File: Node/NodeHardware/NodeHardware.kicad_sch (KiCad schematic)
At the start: 61 parts, among them J1 USB_C_Receptacle_USB2.0_16P, J2 PWR, J3 BATT, Q1 AO3401A, Q2 AO3401A, U1 TPS565201DDCR, U2 TPS565201DDCR, U3 CH340C, U4 TLV70433DBVR, U5 MCP73831-2-OT

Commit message: Finish all the basic SCHM needed for the ESP32
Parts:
- removed C11, C4: C_, symbol Device:C_Polarized
- removed C13, C2, C9: C, Capacitor_SMD:C_0805_2012Metric, symbol Device:C
- removed D4: 5V1, Diode_SMD:D_SOD-123, symbol Device:D_Zener
- removed JP1, JP2, JP3, JP4, JP5, JP6, JP7, JP8: SolderJumper_2_Bridged, Jumper:SolderJumper-2_P1.3mm_Bridged2Bar_RoundedPad1.0x1.5mm, symbol Jumper:SolderJumper_2_Bridged
- removed Q2: AO3401A, Package_TO_SOT_SMD:SOT-23, symbol Transistor_FET:AO3401A
- removed R12: R, Resistor_SMD:R_0805_2012Metric, symbol Device:R
- added C11, C19, C4: 1u, Capacitor_SMD:C_0805_2012Metric, symbol Device:C
- added C2, C9: 100u, symbol Device:C_Polarized
- added C20: 100n, Capacitor_SMD:C_0805_2012Metric, symbol Device:C
- added C22, C23: 4u7, Capacitor_SMD:C_0805_2012Metric, symbol Device:C
- added D12: 5V1, Diode_SMD:D_SOD-123, symbol Device:D_Zener
- added D4: BLUE, LED_SMD:LED_1210_3225Metric, symbol Device:LED
- added J4: ESP32_JTAG, symbol Connector_Generic:Conn_01x07
- added Q5: AO3401A, Package_TO_SOT_SMD:SOT-23, symbol Transistor_FET:AO3401A
- added R15, R18: 47k, Resistor_SMD:R_0805_2012Metric, symbol Device:R
- added R25, R26, R28, R30, R31, R32, R33, R40: 0R, Resistor_SMD:R_0805_2012Metric, symbol Device:R
- added R27: 4k7, Resistor_SMD:R_0805_2012Metric, symbol Device:R
- added R29: 10k, Resistor_SMD:R_0805_2012Metric, symbol Device:R
- C1, C12, C8: value C -> 100n
- C10, C3, C6: value C -> 10u
- C5: value C_ -> 100u
- C7: value C -> 1u
- D2: Part Name (none) -> BZT52C4V7
- H1, H2, H3, H4: footprint (none) -> MountingHole:MountingHole_3.2mm_M3_Pad_Via
- J1: value USB_C_Receptacle_USB2.0_16P -> USB_C_Receptacle_16P
- L1, L2: value L -> 3.3uH
- R1, R4, R9: value R -> 10k
- R10, R11: value R -> 5k1
- R2: value R -> 54.9k
- R3: value R -> 0R; Use Case (none) -> JUMPER
- R5: value R -> 47k
- R6: value R -> ???
- R7: value R -> 4k7
- R8: value R -> 2k2
- TP1: value TestPoint -> 5V_TP
- TP2: value TestPoint -> V_IN_TP
- TP3: value TestPoint -> GND_TP_1
- TP4: value TestPoint -> GND_TP_2
- TP5: value TestPoint -> GND_TP_3
- TP6: value TestPoint -> GND_TP_4
- TP7: value TestPoint -> 3V3_TP
- TP8: value TestPoint -> 3V3_LP_TP
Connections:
- net BATT_N is gone; now on net GND: J3.1 (Pin_1)
- net PWR_IN_N is gone; now on net GND: J2.1 (Pin_1)
- net +5V: now also C3.1, D1.2 (A), L1.2, R2.1, R3.2, TP1.1, U5.4 (V_{DD}), C2.1, C23.1, C4.1, D4.2 (A), R25.1
- net +BATT: now also U5.3 (V_{BAT}), C20.1, C22.1, D12.1 (K), Q5.2 (S), R28.1
- net BATT_P: now also Q5.3 (D)
- net GND: now also C10.2, C12.2, C3.2, C5.2, C6.2, C7.2, H1.1, H2.1, H3.1, H4.1, J1.A1 (GND), J1.A12 (GND), J1.B1 (GND), J1.B12 (GND), R10.2, R11.2, R4.2, R5.2, R7.2, R9.2, TP3.1, TP4.1, TP5.1, TP6.1, U1.1 (GND), U2.1 (GND), U3.1 (GND), U4.1 (GND), U5.2 (V_{SS}), C11.2, C19.2, C2.2, C20.2, C22.2, C23.2, C4.2, C9.2, J4.1 (Pin_1), R15.2, R18.2, R27.2
- net PWR_IN_P: now also Q1.3 (D)
- net VBUS: now also J1.A4 (VBUS), J1.A9 (VBUS), J1.B4 (VBUS), J1.B9 (VBUS), R3.1
- net V_IN: now also C5.1, C6.1, C7.1, D2.1 (K), Q1.2 (S), TP2.1, R26.1
- net net_lable: now also U3.2 (TXD), U3.3 (RXD), U4.2 (IN), R28.2, R32.1, R33.1
- net +3V3_LP: now reaches TP8.1
- net +3V3_LP: now also U4.3 (OUT), C19.1
- net 3V3_REG_VFB: now reaches R9.1
- net 3V3_REG_VFB: now also R6.2, U2.4 (VFB)
- net +3V3: now reaches TP7.1
- net +3V3: now also C10.1, C12.1, D3.2 (A), L2.2, R6.1, U3.16 (VCC), U3.4 (V3), C11.1, C9.1, J4.7 (Pin_7)
- net PWR_IN_ZENER: now reaches R5.1
- net PWR_IN_ZENER: now also D2.2 (A), Q1.1 (G)
- net 5V_REG_VFB: now reaches R4.1
- net 5V_REG_VFB: now also R2.2, U1.4 (VFB)
- net at R10.1: now also J1.A5 (CC1)
- net 3V3_REG_SW: now reaches U2.2 (SW)
- net 3V3_REG_SW: now also C8.1, L2.1
- net 3V3_REG_IN: now reaches U2.3 (VIN)
- net 3V3_REG_IN: now also R25.2, R29.1
- net 3V3_REG_EN: now reaches U2.5 (EN)
- net 3V3_REG_EN: now also R29.2
- net at U2.6 (VBST): now also C8.2
- net 5V_REG_SW: now reaches U1.2 (SW)
- net 5V_REG_SW: now also C1.1, L1.1
- net 5V_REG_IN: now reaches U1.3 (VIN)
- net 5V_REG_IN: now also R1.1, R26.2
- net 5V_REG_EN: now reaches U1.5 (EN)
- net 5V_REG_EN: now also R1.2
- net at U1.6 (VBST): now also C1.2
- net at R8.1: now also U5.1 (STAT)
- net BATT_LED_K: now reaches R8.2
- net BATT_LED_K: now also D4.1 (K)
- net 5V_REG_LED_K: now reaches D1.1 (K)
- net 5V_REG_LED_K: now also R27.1
- net CH340_DTR: now reaches U3.13 (~{DTR})
- net CH340_RTS: now reaches U3.14 (~{RTS})
- net CH340_USB_D+: now reaches U3.5 (UD+)
- net CH340_USB_D+: now also R30.2
- net CH340_USB_D-: now reaches U3.6 (UD-)
- net CH340_USB_D-: now also R31.2
- net 3V3_REG_LED_K: now reaches D3.1 (K)
- net 3V3_REG_LED_K: now also R7.1
- net at U5.5 (PROG): now also R40.1
- net at R11.1: now also J1.B5 (CC2)
- net USB_D+: now reaches J1.A6 (D+), J1.B6 (D+)
- net USB_D+: now also R30.1
- net USB_D-: now reaches J1.A7 (D-), J1.B7 (D-)
- net USB_D-: now also R31.1
- new net: R18.1, R40.2
- new net BATT_IN_ZENER: D12.2 (A), Q5.1 (G), R15.1
- new net JTAG_RST: J4.6 (Pin_6)
- new net JTAG_TCK: J4.5 (Pin_5)
- new net JTAG_TDI: J4.3 (Pin_3)
- new net JTAG_TDO: J4.4 (Pin_4)
- new net JTAG_TMS: J4.2 (Pin_2)
- new net UART_UC_RX: R32.2
- new net UART_UC_TX: R33.2
- no-connect marks 3 -> 11
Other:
- note added: "3V3 BUCK REGULATOR"
- note added: "5V BUCK REGULATOR"
- note added: "Charging can be disabled by removing the PROG jumper. Charging current regulated by PROG resistor: I_reg = 1000V / R_prog (where R_prog is in kOhm) So for 500mA charging, we need 2kOhm resistor."
- note added: "Charging indicator"
- note added: "Debug connection"
- note added: "Low power 3V3 regulator"
- note added: "Power inputs"
- note added: "TODO: Screw terminal (or similar) output pins, with LED indicators of activation (all selectable with one jumper - so we can disable it for ultra low power mode)"
- note added: "TODO: add a symbol and footprint for logo"
- note added: "TODO: add jumpers for power connections for ICs, and jumpers to be able to disconnect anything if needed!"
- note added: "USB C Connector"
- note added: "USB TO UART"
- note added: "Up to 150mA @ 3V3 (3.4μA quiescent current)"
- note added: "What batteries, what configuration, estimated power consumption?"
- note added: "What range of input voltages can we take? What is maximum curr. capability for the PSU selection?"
- note removed: "3V3 regulator"
- note removed: "5V regulator"
- note removed: "LDO, low power 3V3"
- note removed: "Screw terminal (or similar) output pins, with LED indicators of activation (all selectable with one jumper - so we can disable it for ultra low power mode)"
- note removed: "TODO: add JTAG debug connector, power connectors, battery connector..."
- note removed: "TODO: add ground test points"
- note removed: "What range of input voltages can we take?"
- moved on the sheet: C1, D1, D2, H1, H2, H3, H4, J1, J2, J3, L1, Q1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

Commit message: Finish first version of inputs
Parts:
- added R11, R4: INF, Resistor_SMD:R_0805_2012Metric, symbol Device:R
- added R13, R22: 0R, Resistor_SMD:R_0805_2012Metric, symbol Device:R
- renumbered C23 to C13, C19 to C14, C20 to C15, C22 to C16, C5 to C2, C6 to C3, C7 to C4, C2 to C5, C3 to C6, C4 to C7, D12 to D5, J4 to J3, J3 to J4, Q5 to Q2, R26 to R1, R6 to R10, R7 to R12, R3 to R14, R9 to R15, R10 to R16, R32 to R17, R11 to R18, R33 to R19, R1 to R2, R30 to R20, R31 to R21, R8 to R23, R28 to R24, R40 to R25, R15 to R26, R18 to R27, R2 to R3, R27 to R6, R4 to R7, R25 to R8, R29 to R9, TP2 to TP1, TP1 to TP2
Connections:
- net +3V3: now also R13.1; no longer C12.1, U3.16 (VCC), U3.4 (V3)
- net +5V: now also R22.2; no longer C13.1, D4.2 (A), U5.4 (V_{DD})
- net +BATT: no longer C16.1, U5.3 (V_{BAT})
- net 3V3_REG_EN: now also R11.2
- net 5V_REG_EN: now also R4.2
- net BATT_P: now also C16.1, U5.3 (V_{BAT})
- net GND: now also R11.1, R4.1
- net net_lable: no longer R24.2, U4.2 (IN)
- new net: C12.1, R13.2, U3.16 (VCC), U3.4 (V3)
- new net: C13.1, D4.2 (A), R22.1, U5.4 (V_{DD})
- new net 3V3_LP_REG_IN: R24.2, U4.2 (IN)
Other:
- note added: "1 Cell LiIon battery"
- note added: "Input: 6V to 17V"
- note added: "We can disable this regulator if needed"
- note removed: "What batteries, what configuration, estimated power consumption?"
- note removed: "What range of input voltages can we take? What is maximum curr. capability for the PSU selection?"
- moved on the sheet: C13, C14, C15, C16, D4, J4, R23, TP8, U4

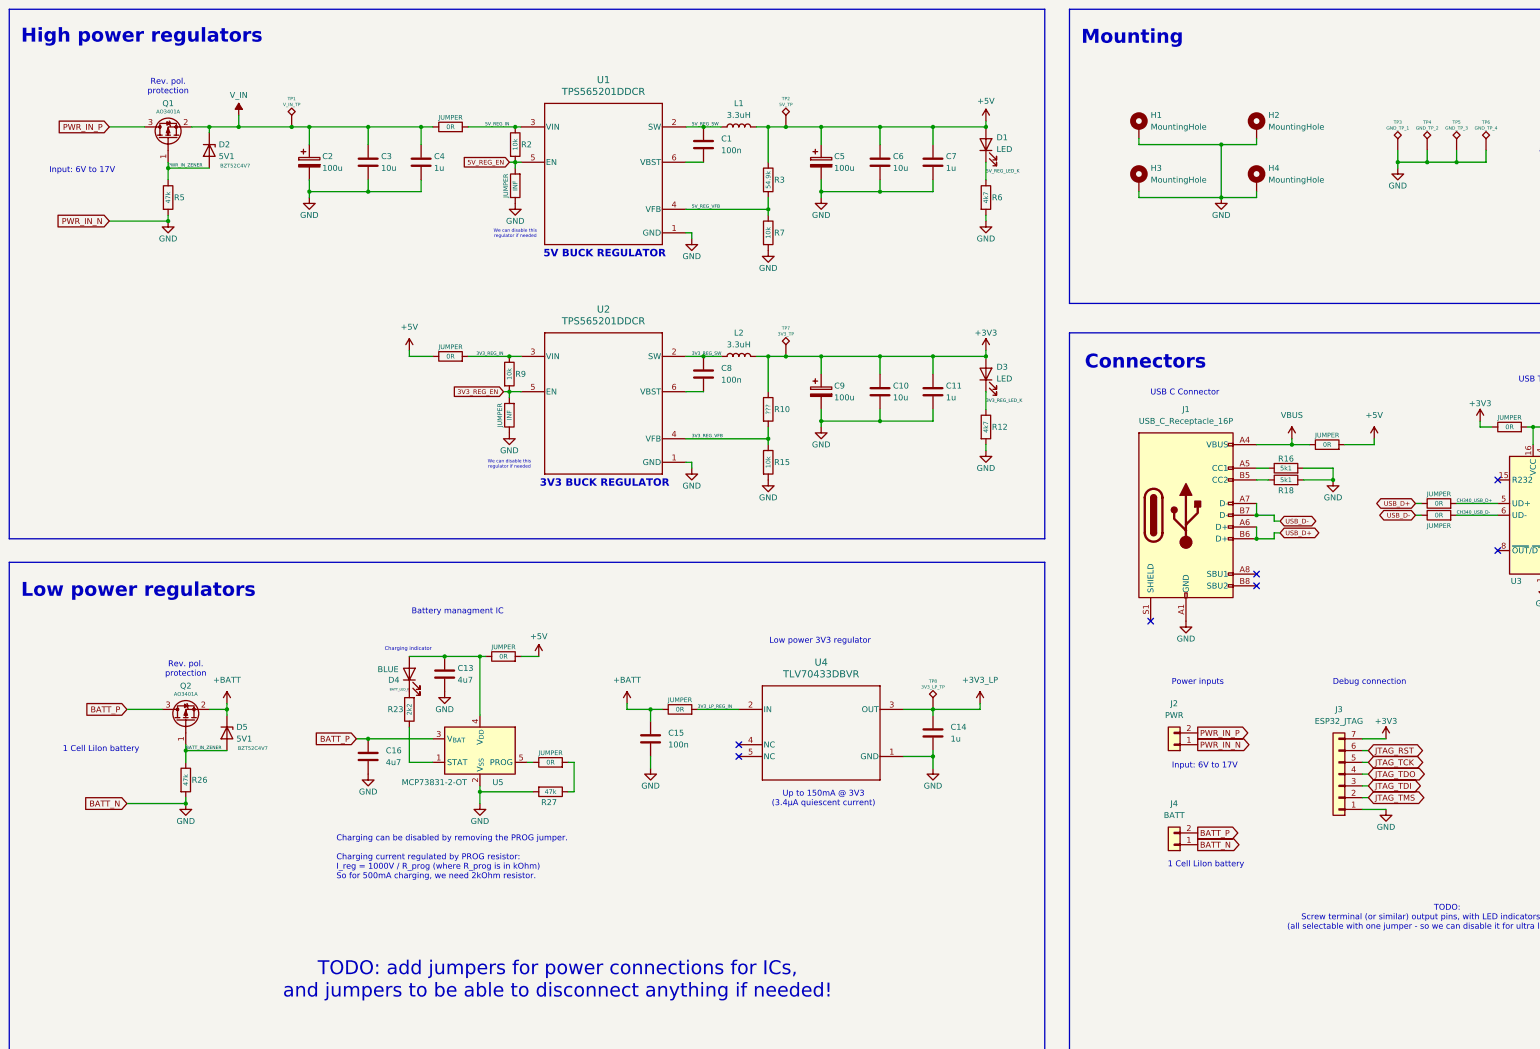
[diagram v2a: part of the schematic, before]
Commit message: added some comments and sim module to schematic
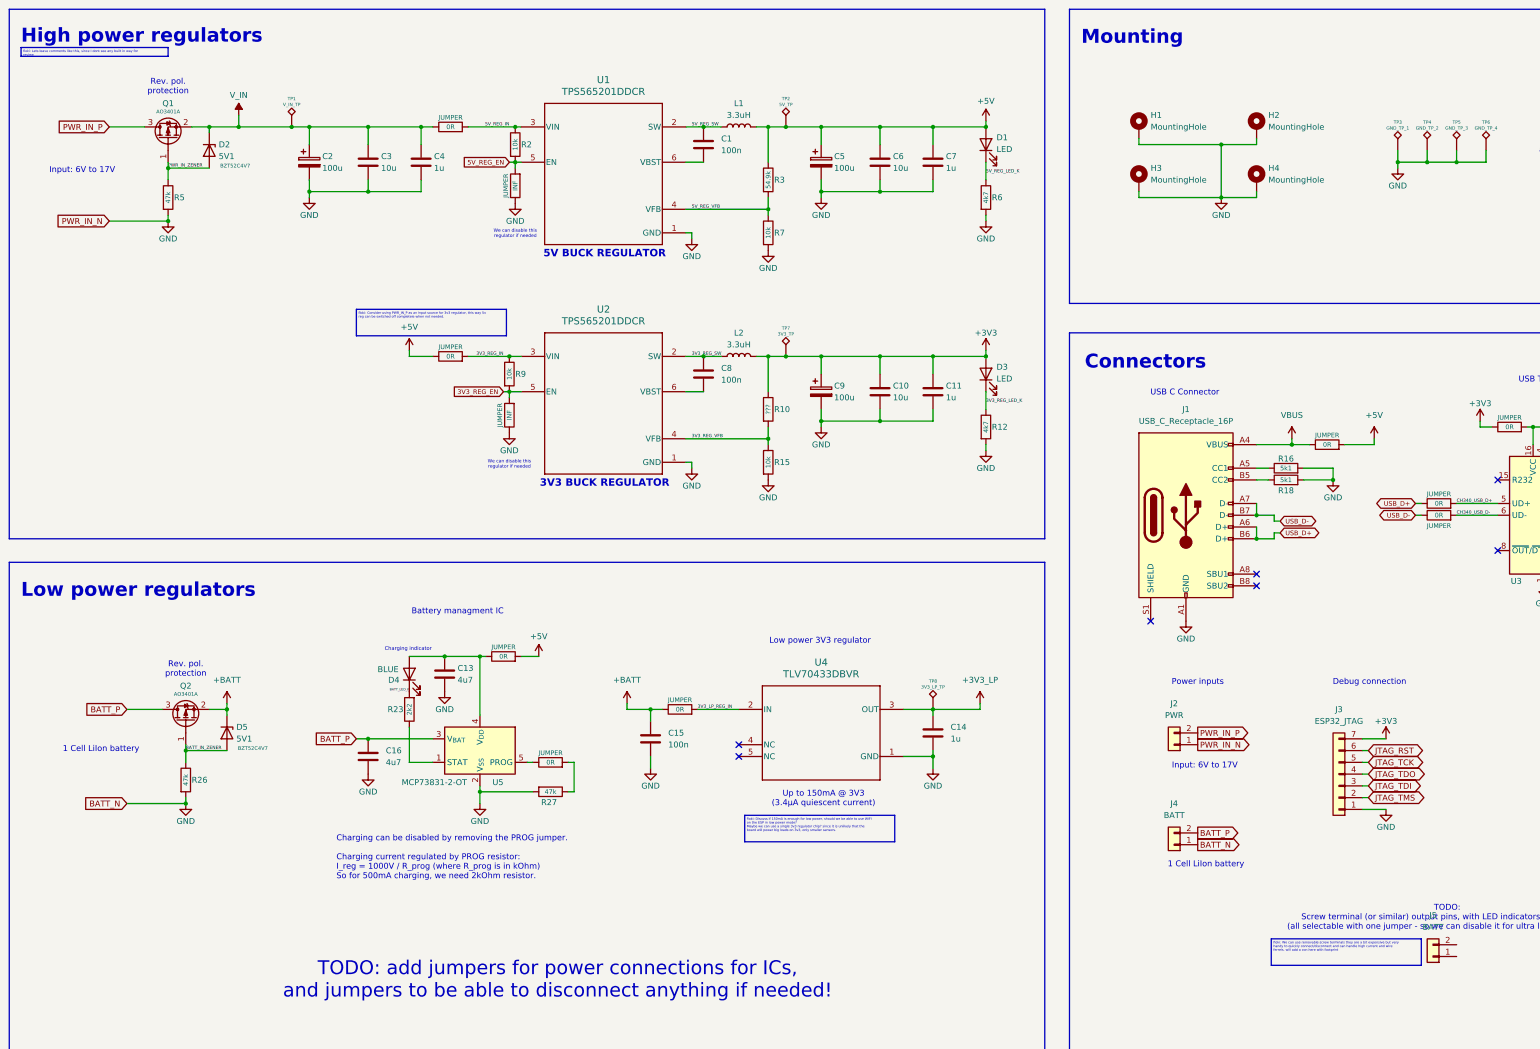
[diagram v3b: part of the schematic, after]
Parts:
- added J5: BATT, fflori4nComponents:TerminalBlockRemovablex2_Silk, symbol Connector_Generic:Conn_01x02
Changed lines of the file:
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@@
+		)
+	)
+	(text_box "floki: We can use removable screw terminals they are a bit expensive but very handy to quickly connect/disconnect and can handle high current and wire ferrels. will add a con here with footprint\n"
+		(exclude_from_sim no)
+		(at 288.925 217.17 0)
+		(size 32.385 5.715)
+		(stroke
+			(width 0)
+			(type default)
+		)
+		(fill
+			(type color)
+			(color 255 0 17 1)
+		)
+		(effects
+			(font
+				(size 0.5 0.5)
+			)
+			(justify left top)
+		)
+	)
+	(text_box "floki: Lets leave comments like this, since I dont see any built in way for review"
+		(exclude_from_sim no)
+		(at 19.05 24.765 0)
+		(size 31.75 1.905)
+		(stroke
+			(width 0)
+			(type default)
+		)
+		(fill
+			(type color)
+			(color 255 0 17 1)
+		)
+		(effects
+			(font
+				(size 0.5 0.5)
+			)
+			(justify left top)
+		)
+	)
+	(text_box "floki: Consider using PWR_IN_P as an input source for 3v3 regulator, this way 5v reg can be switched off completele when not needed."
+		(exclude_from_sim no)
+		(at 91.44 81.28 0)
+		(size 32.385 5.715)
+		(stroke
+			(width 0)
+			(type default)
+		)
+		(fill
+			(type color)
+			(color 255 0 17 1)
+		)
+		(effects
+			(font
+				(size 0.5 0.5)
+			)
+			(justify left top)
+		)
+	)
+	(text_box "floki: Discuss if 150mA is enough for low power, should we be able to use WiFi on the ESP in low power mode?\nMaybe we can use a single 3v3 regulator chip? since it is unlikely that the board will power big loads on 3v3, only smaller sensors."
+		(exclude_from_sim no)
+		(at 175.26 190.5 0)
+		(size 32.385 5.715)
+		(stroke
+			(width 0)
+			(type default)
+		)
+		(fill
+			(type color)
+			(color 255 0 17 1)
+		)
+		(effects
+			(font
+				(size 0.5 0.5)
+			)
+			(justify left top)
 		)
 	)
@@
 					(unit 1)
 				)
+			)
+		)
+	)
+	(symbol
+		(lib_id "Connector_Generic:Conn_01x02")
+		(at 323.85 220.98 180)
+		(unit 1)
+		(exclude_from_sim no)
+		(in_bom yes)
+		(on_board yes)
+		(dnp no)
+		(fields_autoplaced yes)
+		(property "Reference" "J5"
+			(at 323.85 212.09 0)
+			(effects
+				(font
+					(size 1.27 1.27)
+				)
+			)
+		)
+		(property "Value" "BATT"
+			(at 323.85 214.63 0)
+			(effects
+				(font
+					(size 1.27 1.27)
+				)
+			)
+		)
+		(property "Footprint" "fflori4nComponents:TerminalBlockRemovablex2_Silk"
+			(at 323.85 220.98 0)
+			(effects
+				(font
+					(size 1.27 1.27)
+				)
+				(hide yes)
+			)
+		)
+		(property "Datasheet" "~"
+			(at 323.85 220.98 0)
+			(effects
+				(font
+					(size 1.27 1.27)
+				)
+				(hide yes)
+			)
+		)
+		(property "Description" "Generic connector, single row, 01x02, script generated (kicad-library-utils/schlib/autogen/connector/)"
+			(at 323.85 220.98 0)
+			(effects
+				(font
+					(size 1.27 1.27)
+				)
+				(hide yes)
+			)
+		)
+		(pin "2"
+		)
+		(pin "1"
+		)
+		(instances
+			(project "NodeHardware"
+				(path "/fbf6e9fb-8cea-4ffc-9c5e-2f0b106da475"
+					(reference "J5")
+					(unit 1)
+				)

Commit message: Schm cleanup and commenting
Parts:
- removed J2: PWR, symbol Connector_Generic:Conn_01x02
- added C36: 470u, symbol Device:C_Polarized
- added C37: 100u, symbol Device:C_Polarized
- added C38: 10u, Capacitor_SMD:C_0805_2012Metric, symbol Device:C
- added U9: SIM7000G_DEVBoard, myComponents:sim7000G_dev_board_rev3, symbol myComponents:SIM7000G_DEVBoard
- J4: value BATT -> PWR_IN; footprint (none) -> fflori4nComponents:TerminalBlockRemovablex2_Silk
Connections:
- net +5V: now also C36.1, C37.1, C38.1, U9.2 (POWER)
- net BATT_P: now also J5.2 (Pin_2); no longer J4.2 (Pin_2)
- net GND: now also J5.1 (Pin_1), C36.2, C37.2, C38.2, U9.3 (GND), U9.5 (GND)
- net PWR_IN_P: now also J4.2 (Pin_2)
- net UART_UC_RX: now also U9.8 (TXD)
- net UART_UC_TX: now also U9.6 (RXD)
- new net +3.3V: U9.7 (V_MCU)
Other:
- note added: "GSM module connection"
- note removed: "Charging can be disabled by removing the PROG jumper. Charging current regulated by PROG resistor: I_reg = 1000V / R_prog (where R_prog is in kOhm) So for 500mA charging, we need 2kOhm resistor."
- note removed: "TODO: GSM module connector (most likely just UART and power)"
- note removed: "TODO: add jumpers for power connections for ICs, and jumpers to be able to disconnect anything if needed!"
- note removed: "We can disable this regulator if needed"
- moved on the sheet: J3, J5

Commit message: Update SCHM (psu, cleanup), add datasheets
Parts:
- removed C10: 10u, Capacitor_SMD:C_0805_2012Metric, symbol Device:C
- removed C11: 1u, Capacitor_SMD:C_0805_2012Metric, symbol Device:C
- removed C8: 100n, Capacitor_SMD:C_0805_2012Metric, symbol Device:C
- removed C9: 100u, symbol Device:C_Polarized
- removed D3: LED, LED_SMD:LED_1210_3225Metric, symbol Device:LED
- removed D5: 5V1, Diode_SMD:D_SOD-123, symbol Device:D_Zener
- removed L2: 3.3uH, symbol Device:L
- removed R10: ???, Resistor_SMD:R_0805_2012Metric, symbol Device:R
- removed R11: INF, Resistor_SMD:R_0805_2012Metric, symbol Device:R
- removed R12: 4k7, Resistor_SMD:R_0805_2012Metric, symbol Device:R
- removed R15, R9: 10k, Resistor_SMD:R_0805_2012Metric, symbol Device:R
- removed R26: 47k, Resistor_SMD:R_0805_2012Metric, symbol Device:R
- removed U2: TPS565201DDCR, TPS565201DDCR:TPS565201DDCR_L, symbol TPS565201DDCR:TPS565201DDCR
- removed U4: TLV70433DBVR, TLV70433DBVR:DBV0005A_L, symbol TLV70433DBVR:TLV70433DBVR
- added D3: SS14, Diode_SMD:D_SMA, symbol Diode:SS14
- added J10: PWR_OUT_5V, symbol Connector_Generic:Conn_01x04
- added J11: PWR_OUT_3V3, symbol Connector_Generic:Conn_01x04
- added J7: DIG_IO_A, symbol Connector_Generic:Conn_01x06
- added J8: DIG_IO_B, symbol Connector_Generic:Conn_01x06
- added J9: ANA_IN, symbol Connector_Generic:Conn_01x08
- added U2: SPX3819M5-L-3-3, Package_TO_SOT_SMD:SOT-23-5, symbol Regulator_Linear:SPX3819M5-L-3-3
- TP7: value 3V3_TP -> 3V3_Bypass_TP
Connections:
- net 3V3_REG_IN is gone; now on net 3V3_LP_REG_IN: R8.2
- net BATT_IN_ZENER is gone; now on net GND: Q2.1 (G)
- net +3V3: no longer TP7.1
- net +3V3_LP: now also J11.1 (Pin_1), J11.2 (Pin_2), J11.3 (Pin_3), J11.4 (Pin_4), U2.5 (OUT)
- net +5V: now also J10.1 (Pin_1), J10.2 (Pin_2), J10.3 (Pin_3), J10.4 (Pin_4); no longer R8.1
- net +BATT: now also D3.1 (K)
- net 3V3_LP_REG_IN: now also U2.1 (IN)
- net BATT_P: now also D3.2 (A)
- net GND: now also J7.1 (Pin_1), J7.3 (Pin_3), J7.5 (Pin_5), J8.1 (Pin_1), J8.3 (Pin_3), J8.5 (Pin_5), J9.1 (Pin_1), J9.3 (Pin_3), J9.5 (Pin_5), J9.7 (Pin_7), U2.2 (GND)
- new net: R8.1, U2.3 (EN)
- new net: TP7.1, U2.4 (BP)
- new net ANA_IN_01: J9.2 (Pin_2)
- new net ANA_IN_02: J9.4 (Pin_4)
- new net ANA_IN_03: J9.6 (Pin_6)
- new net ANA_IN_04: J9.8 (Pin_8)
- new net DIG_IO_01: J7.2 (Pin_2)
- new net DIG_IO_02: J7.4 (Pin_4)
- new net DIG_IO_03: J7.6 (Pin_6)
- new net DIG_IO_04: J8.2 (Pin_2)
- new net DIG_IO_05: J8.4 (Pin_4)
- new net DIG_IO_06: J8.6 (Pin_6)
- no-connect marks 11 -> 9
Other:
- note added: "1 Cell Li-Ion battery"
- note added: "Analog Inputs"
- note added: "Backup instead of PMOS Vf = 0.50 - 0.75 V"
- note added: "Digital IO"
- note added: "EN pin: HIGH = ON LOW/OPEN = OFF"
- note added: "Miniature Single-Cell, Fully Integrated Li-Ion/Li-Polymer Charge Management Controller"
- note added: "RDS(ON) ＜ 120mΩ (VGS =-2.5V) V GS(th) = -0.4V .. -1.3V"
- note added: "Up to 500mA @ 3V3 Low dropout: 340mV at full load (90μA quiescent current)"
- note removed: "3V3 BUCK REGULATOR"
- note removed: "TODO: Screw terminal (or similar) output pins, with LED indicators of activation (all selectable with one jumper - so we can disable it for ultra low power mode)"
- note removed: "TODO: add a symbol and footprint for logo"
- note removed: "TODO: add a symbol and footprint for mounting case (box drawing, with holes and all)"
- note removed: "Up to 150mA @ 3V3 (3.4μA quiescent current)"
- moved on the sheet: C12, C13, C14, C15, C16, C36, C37, C38, D4, J1, J3, J4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
